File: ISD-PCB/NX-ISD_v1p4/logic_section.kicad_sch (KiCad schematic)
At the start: 7 parts, among them U13 ESP32-S3-WROOM-1-N16R8

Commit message: feat(pcb): v1.4 schematic and layout updates for 4-bit SDMMC, direct display SPI, and button pullups
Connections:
- net !INT_ALS is gone; now on net SCK: U13.32 (IO39)
- net !INT_H is gone; now on net CS_SD: U13.38 (IO2)
- net CS_SD: no longer U13.24 (IO47)
- net MOSI: now also U13.33 (IO40); no longer U13.35 (IO42)
- net PWM_TFT: now also U13.24 (IO47); no longer U13.39 (IO1)
- net SCK: no longer U13.33 (IO40)
- net SD_DAT1: now reaches U13.36 (RXD0)
- net SD_DAT0: now reaches U13.37 (TXD0)
- net !INT_DOF: now reaches U13.7 (IO7)
- net MISO renamed SD_CLK
- new net SD_CMD: U13.39 (IO1)
- new net SD_DAT2: U13.35 (IO42)
- no-connect marks 9 -> 6
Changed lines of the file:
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@@
-	)
-	(no_connect
-		(at 86.36 48.26)
 	)
 	(no_connect
@@
 	)
 	(no_connect
-		(at 86.36 45.72)
-	)
-	(no_connect
 		(at 86.36 83.82)
 	)
-	(no_connect
-		(at 55.88 68.58)
-	)
 	(wire
 		(pts
@@
 	(wire
 		(pts
+			(xy 38.1 68.58) (xy 55.88 68.58)
+		)
+		(stroke
+			(width 0)
+			(type default)
+		)
+	)
+	(wire
+		(pts
+			(xy 86.36 45.72) (xy 101.6 45.72)
+		)
+		(stroke
+			(width 0)
+			(type default)
+		)
+	)
+	(wire
+		(pts
 			(xy 71.12 35.56) (xy 71.12 40.64)
 		)
@@
 	(wire
 		(pts
+			(xy 86.36 48.26) (xy 101.6 48.26)
+		)
+		(stroke
+			(width 0)
+			(type default)
+		)
+	)
+	(wire
+		(pts
 			(xy 36.83 120.65) (xy 43.18 120.65)
 		)
@@
 	(wire
 		(pts
+			(xy 86.36 78.74) (xy 101.6 78.74)
+		)
+		(stroke
+			(width 0)
+			(type default)
+		)
+	)
+	(wire
+		(pts
 			(xy 38.1 60.96) (xy 55.88 60.96)
 		)
@@
 	(wire
 		(pts
+			(xy 86.36 76.2) (xy 101.6 76.2)
+		)
+		(stroke
+			(width 0)
+			(type default)
+		)
+	)
+	(wire
+		(pts
 			(xy 137.16 55.88) (xy 140.97 55.88)
 		)
@@
 	(wire
 		(pts
-			(xy 86.36 76.2) (xy 101.6 76.2)
-		)
-		(stroke
-			(width 0)
-			(type default)
-		)
-	)
-	(wire
-		(pts
 			(xy 171.45 63.5) (xy 171.45 68.58)
 		)
@@
 	(wire
 		(pts
+			(xy 38.1 53.34) (xy 55.88 53.34)
+		)
+		(stroke
+			(width 0)
+			(type default)
+		)
+	)
+	(wire
+		(pts
 			(xy 86.36 53.34) (xy 101.6 53.34)
 		)
@@
 	(wire
 		(pts
+			(xy 86.36 81.28) (xy 101.6 81.28)
+		)
+		(stroke
+			(width 0)
+			(type default)
+		)
+	)
+	(wire
+		(pts
 			(xy 38.1 86.36) (xy 55.88 86.36)
 		)
@@
 	(wire
 		(pts
+			(xy 55.88 55.88) (xy 38.1 55.88)
+		)
+		(stroke
+			(width 0)
+			(type default)
+		)
+	)
+	(wire
+		(pts
 			(xy 36.83 110.49) (xy 43.18 110.49)
 		)
@@
 	(wire
 		(pts
-			(xy 86.36 78.74) (xy 101.6 78.74)
-		)
-		(stroke
-			(width 0)
-			(type default)
-		)
-	)
-	(wire
-		(pts
 			(xy 147.32 64.77) (xy 147.32 68.58)
 		)
@@
 	(wire
 		(pts
-			(xy 38.1 55.88) (xy 55.88 55.88)
-		)
-		(stroke
-			(width 0)
-			(type default)
-		)
-	)
-	(wire
-		(pts
 			(xy 43.18 110.49) (xy 43.18 111.76)
 		)
@@
 	(wire
 		(pts
-			(xy 55.88 53.34) (xy 38.1 53.34)
-		)
-		(stroke
-			(width 0)
-			(type default)
-		)
-	)
-	(wire
-		(pts
 			(xy 86.36 91.44) (xy 101.6 91.44)
 		)
@@
 		(pts
 			(xy 147.32 55.88) (xy 147.32 57.15)
-		)
-		(stroke
-			(width 0)
-			(type default)
-		)
-	)
-	(wire
-		(pts
-			(xy 86.36 81.28) (xy 101.6 81.28)
 		)
 		(stroke
@@
 		)
 	)
+	(hierarchical_label "PWM_TFT"
+		(shape output)
+		(at 101.6 88.9 0)
+		(effects
+			(font
+				(size 1.27 1.27)
+			)
+			(justify left)
+		)
+	)
+	(hierarchical_label "SD_DAT2"
+		(shape bidirectional)
+		(at 101.6 81.28 0)
+		(effects
+			(font
+				(size 1.27 1.27)
+			)
+			(justify left)
+		)
+	)
 	(hierarchical_label "LEVER_PUSH"
 		(shape input)
@@
 		)
 	)
-	(hierarchical_label "MOSI"
-		(shape output)
-		(at 101.6 81.28 0)
+	(hierarchical_label "SCK"
+		(shape output)
+		(at 101.6 73.66 0)
 		(effects
 			(font
@@
 		)
 	)
-	(hierarchical_label "!INT_ALS"
-		(shape input)
-		(at 101.6 73.66 0)
-		(effects
-			(font
-				(size 1.27 1.27)
-			)
-			(justify left)
-		)
-	)
 	(hierarchical_label "BAT_STAT"
 		(shape input)
 		(at 38.1 78.74 180)
+		(effects
+			(font
+				(size 1.27 1.27)
+			)
+			(justify right)
+		)
+	)
+	(hierarchical_label "CS_SD"
+		(shape bidirectional)
+		(at 38.1 55.88 180)
 		(effects
 			(font
@@
 		)
 	)
+	(hierarchical_label "SD_CLK"
+		(shape output)
+		(at 101.6 78.74 0)
+		(effects
+			(font
+				(size 1.27 1.27)
+			)
+			(justify left)
+		)
+	)
+	(hierarchical_label "SD_DAT1"
+		(shape bidirectional)
+		(at 101.6 48.26 0)
+		(effects
+			(font
+				(size 1.27 1.27)
+			)
+			(justify left)
+		)
+	)
 	(hierarchical_label "DOUT_NPM"
 		(shape output)
@@
 			)
 			(justify left)
-		)
-	)
-	(hierarchical_label "!INT_H"
-		(shape input)
-		(at 38.1 55.88 180)
-		(effects
-			(font
-				(size 1.27 1.27)
-			)
-			(justify right)
 		)
 	)
@@
 		)
 	)
-	(hierarchical_label "CS_SD"
-		(shape output)
-		(at 101.6 88.9 0)
-		(effects
-			(font
-				(size 1.27 1.27)
-			)
-			(justify left)
+	(hierarchical_label "!INT_DOF"
+		(shape input)
+		(at 38.1 68.58 180)
+		(effects
+			(font
+				(size 1.27 1.27)
+			)
+			(justify right)
 		)
 	)
@@
 		)
 	)
-	(hierarchical_label "MISO"
-		(shape input)
-		(at 101.6 78.74 0)
-		(effects
-			(font
-				(size 1.27 1.27)
-			)
-			(justify left)
-		)
-	)
 	(hierarchical_label "RST"
 		(shape output)
@@
 		)
 	)
-	(hierarchical_label "PWM_TFT"
-		(shape output)
+	(hierarchical_label "SD_CMD"
+		(shape bidirectional)
 		(at 38.1 53.34 180)
 		(effects
@@
 		)
 	)
-	(hierarchical_label "SCK"
+	(hierarchical_label "SD_DAT0"
+		(shape bidirectional)
+		(at 101.6 45.72 0)
+		(effects
+			(font
+				(size 1.27 1.27)
+			)
+			(justify left)
+		)
+	)
+	(hierarchical_label "MOSI"
 		(shape output)
 		(at 101.6 76.2 0)

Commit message: hw(v1.4): progress on TODO - 4-bit MicroSD, direct display bus, BNO085 & EP vias (DRC 0 errors)
- Implemented 4-bit SDMMC MicroSD slot (Molex 105162-0001) on right edge with outward insertion
- Routed direct 3.3V display SPI bus (TE 1-2328702-0) with C29 100nF decoupling
- Centered BNO085 9-DOF IMU cluster with local ground star and 32.768kHz crystal
- Rerouted NeoPixel PWR_NPM high-side power gate signal
- Updated thermal EP pad via sizes on BQ25170 and MAX17048 for standard JLCPCB fabrication
- Achieved 0 DRC errors, 0 unconnected nets, and 100% schematic parity
- Updated HW-TODO and SW-TODO for v1.3/v1.4 pinout target abstraction
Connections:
- net MOSI: now also U13.32 (IO39); no longer U13.33 (IO40)
- net RST: now also U13.33 (IO40); no longer U13.31 (IO38)
- net SCK: now also U13.31 (IO38); no longer U13.32 (IO39)
- net SD_CMD: now also U13.37 (TXD0); no longer U13.39 (IO1)
- net SD_DAT0: now also U13.36 (RXD0); no longer U13.37 (TXD0)
- net SD_DAT1: now also U13.35 (IO42); no longer U13.36 (RXD0)
- net SD_DAT2: now also U13.39 (IO1); no longer U13.35 (IO42)

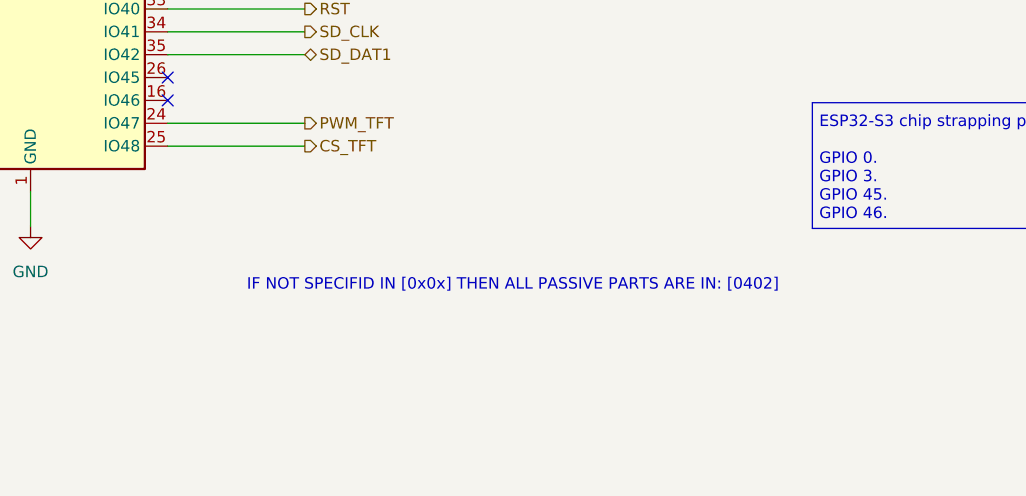
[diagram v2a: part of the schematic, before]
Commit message: hw(v1.4): bq25170 thermal optimization, usb-c plating, battery pad stitching, and npm decoupling
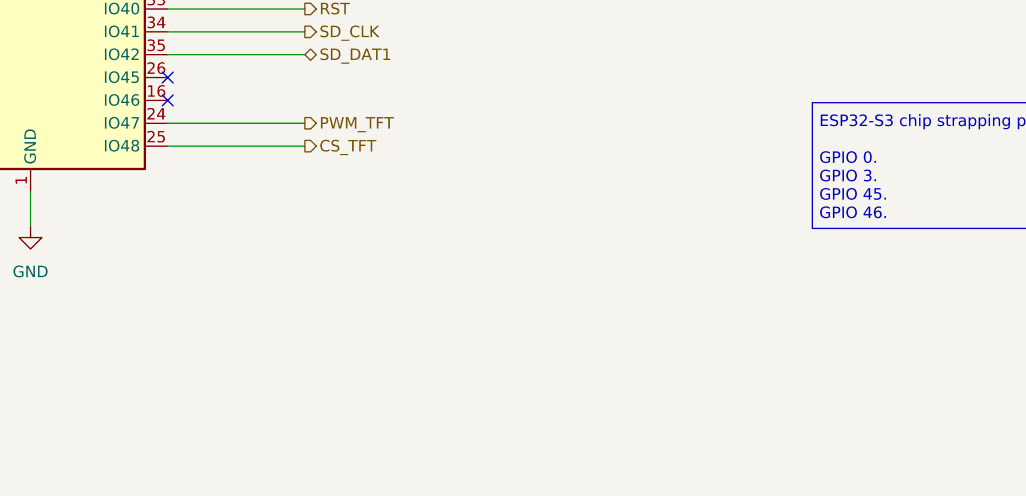
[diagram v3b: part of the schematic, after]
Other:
- note removed: "IF NOT SPECIFID IN [0x0x] THEN ALL PASSIVE PARTS ARE IN: [0402]"
- title: (none) -> NX-ISD Version 1 Rev. 4
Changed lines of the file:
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@@
 	(generator_version "10.0")
 	(paper "A5")
+	(title_block
+		(title "NX-ISD Version 1 Rev. 4")
+		(date "2026-10-16")
+		(rev "p4")
+		(comment 1 "IF NOT SPECIFID IN [0x0x] THEN ALL PASSIVE PARTS ARE IN: [0402]")
+	)
 	(rectangle
 		(start 157.988 86.614)
@@
 		)
 	)
-	(text "IF NOT SPECIFID IN [0x0x] THEN ALL PASSIVE PARTS ARE IN: [0402]"
-		(exclude_from_sim no)
-		(at 124.714 106.934 0)
-		(effects
-			(font
-				(size 1.27 1.27)
-			)
-		)
-	)

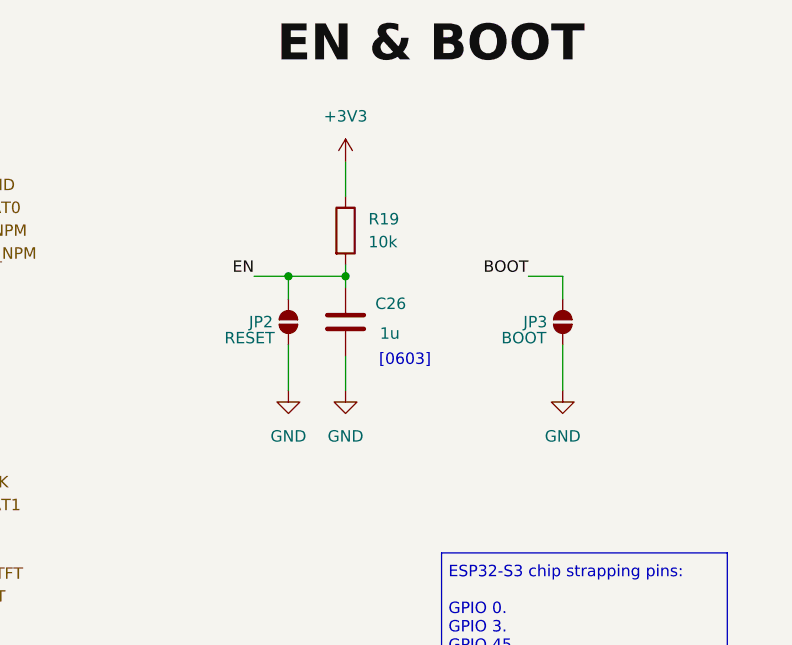
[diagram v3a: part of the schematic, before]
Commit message: hw(v1p4): add RTC backup supercap C27, tactile buttons, USBLC6 footprint adjustments, and cyberpunk silkscreens
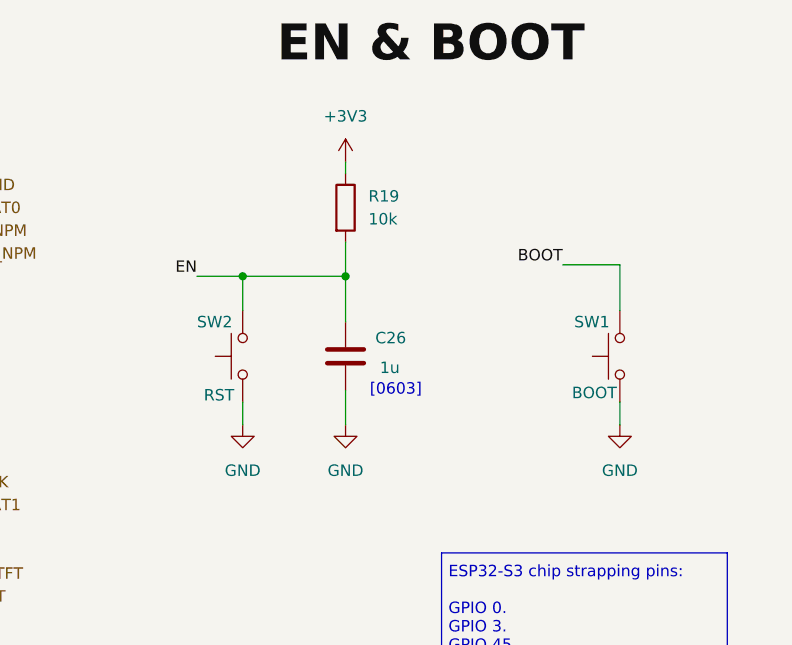
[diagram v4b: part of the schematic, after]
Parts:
- removed JP2: RESET, Jumper:SolderJumper-2_P1.3mm_Open_TrianglePad1.0x1.5mm, symbol Jumper:SolderJumper_2_Open
- removed JP3: BOOT, Jumper:SolderJumper-2_P1.3mm_Open_TrianglePad1.0x1.5mm, symbol Jumper:SolderJumper_2_Open
- added SW1: BOOT, Button_Switch_SMD:SW_SPST_PTS810, symbol Switch:SW_Push
- added SW2: RST, Button_Switch_SMD:SW_SPST_PTS810, symbol Switch:SW_Push
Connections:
- net BOOT: now also SW1.2
- net EN: now also SW2.2
- net GND: now also SW1.1, SW2.1
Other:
- moved on the sheet: C26, R19
